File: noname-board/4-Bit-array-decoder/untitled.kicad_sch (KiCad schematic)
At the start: 16 parts, among them U1 CD4514BM

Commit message: hmmm
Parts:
- removed D1, D10, D11, D12, D13, D14, D15, D2, D3, D4, D5, D6, D7, D8, D9: LED, symbol Device:LED
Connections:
- net leds and resistors cus long/out_pin 13: now reaches U1.16 (S14)
- net leds and resistors cus long/out_pin 11: now reaches U1.19 (S11)
- net leds and resistors cus long/out_pin 8: now reaches U1.9 (S2)
- net leds and resistors cus long/out_pin 7: now reaches U1.8 (S3)
- net leds and resistors cus long/out_pin 10: now reaches U1.20 (S10)
- net leds and resistors cus long/out_pin 4: now reaches U1.18 (S8)
- net leds and resistors cus long/out_pin 9: now reaches U1.10 (S1)
- net leds and resistors cus long/out_pin 14: now reaches U1.13 (S13)
- net leds and resistors cus long/out_pin 12: now reaches U1.14 (S12)
- net leds and resistors cus long/out_pin 15: now reaches U1.15 (S15)
- net leds and resistors cus long/out_pin 5: now reaches U1.17 (S9)
- net leds and resistors cus long/out_pin 6: now reaches U1.4 (S7)
- net leds and resistors cus long/out_pin 2: now reaches U1.5 (S6)
- net leds and resistors cus long/out_pin 3: now reaches U1.6 (S5)
- net leds and resistors cus long/out_pin 1: now reaches U1.7 (S4)
- net power renamed 5V
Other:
- added sheet leds and resistors cus long (leds and resistors cus long.kicad_sch)

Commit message: commented on evan's thing
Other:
- note added: "so real"
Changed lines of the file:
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@@
     (stroke (width 0) (type default))
+  )
+  (text "so real\n" (at 165.1 116.84 0)
+    (effects (font (size 1.27 1.27)) (justify left bottom))
   )
   (global_label "GND" (shape input) (at 128.27 116.84 0) (fields_autoplaced)

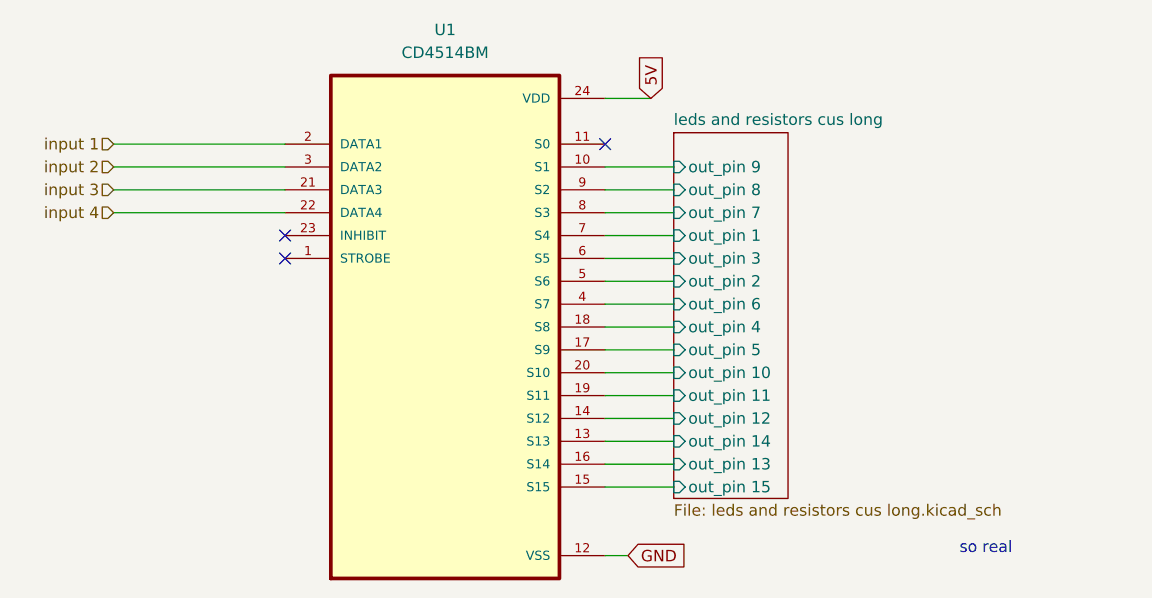
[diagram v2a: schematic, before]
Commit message: Changed Global to Hierarchals
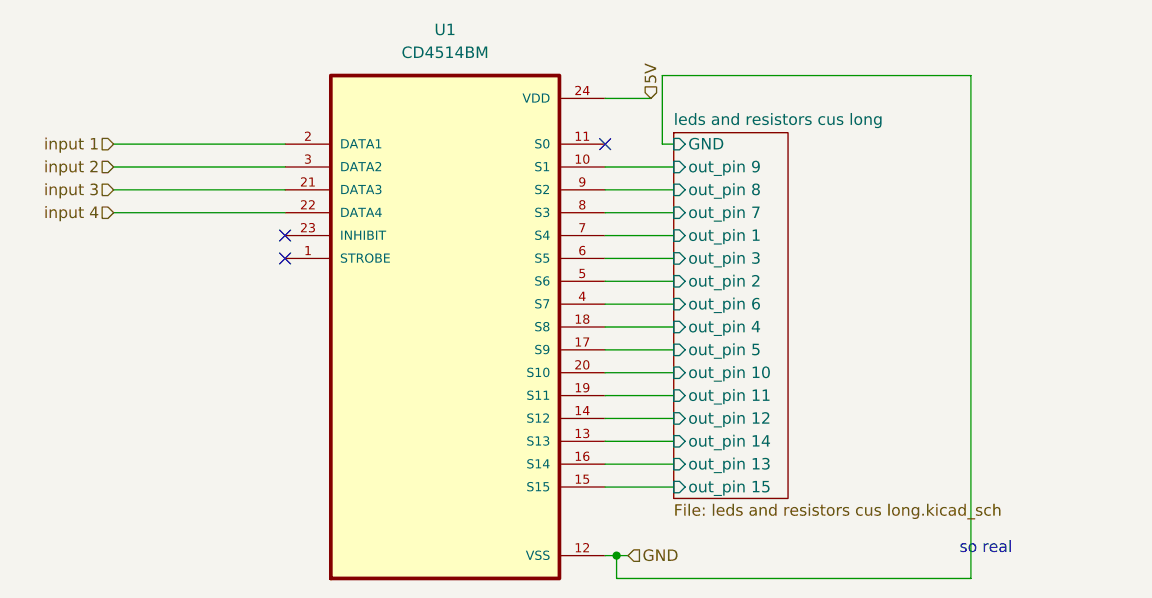
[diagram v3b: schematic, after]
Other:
- sheet leds and resistors cus long ports: added GND; removed none
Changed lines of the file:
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@@
 (kicad_sch (version 20230121) (generator eeschema)
   (paper "A4")
+  (junction (at 127 116.84) (diameter 0) (color 0 0 0 0)
+  )
   (no_connect (at 90.17 83.82))
   (no_connect (at 90.17 81.28))
@@
     (stroke (width 0) (type default))
   )
+  (wire (pts (xy 132.08 63.5) (xy 166.37 63.5))
+    (stroke (width 0) (type default))
+  )
+  (wire (pts (xy 127 116.84) (xy 128.27 116.84))
+    (stroke (width 0) (type default))
+  )
   (wire (pts (xy 125.73 81.28) (xy 133.35 81.28))
     (stroke (width 0) (type default))
@@
     (stroke (width 0) (type default))
   )
+  (wire (pts (xy 132.08 71.12) (xy 132.08 63.5))
+    (stroke (width 0) (type default))
+  )
   (wire (pts (xy 125.73 99.06) (xy 133.35 99.06))
     (stroke (width 0) (type default))
@@
     (stroke (width 0) (type default))
   )
+  (wire (pts (xy 166.37 119.38) (xy 127 119.38))
+    (stroke (width 0) (type default))
+  )
   (wire (pts (xy 125.73 101.6) (xy 133.35 101.6))
     (stroke (width 0) (type default))
@@
     (stroke (width 0) (type default))
   )
+  (wire (pts (xy 127 119.38) (xy 127 116.84))
+    (stroke (width 0) (type default))
+  )
+  (wire (pts (xy 133.35 71.12) (xy 132.08 71.12))
+    (stroke (width 0) (type default))
+  )
   (wire (pts (xy 125.73 109.22) (xy 133.35 109.22))
     (stroke (width 0) (type default))
   )
+  (wire (pts (xy 166.37 63.5) (xy 166.37 119.38))
+    (stroke (width 0) (type default))
+  )
   (wire (pts (xy 125.73 78.74) (xy 133.35 78.74))
     (stroke (width 0) (type default))
   )
-  (wire (pts (xy 125.73 116.84) (xy 128.27 116.84))
+  (wire (pts (xy 125.73 116.84) (xy 127 116.84))
     (stroke (width 0) (type default))
   )
@@
     (effects (font (size 1.27 1.27)) (justify left bottom))
   )
-  (global_label "GND" (shape input) (at 128.27 116.84 0) (fields_autoplaced)
+  (hierarchical_label "GND" (shape input) (at 128.27 116.84 0) (fields_autoplaced)
     (effects (font (size 1.27 1.27)) (justify left))
-    (property "Intersheetrefs" "${INTERSHEET_REFS}" (at 135.1257 116.84 0)
-      (effects (font (size 1.27 1.27)) (justify left) hide)
-    )
-  )
-  (global_label "5V" (shape input) (at 130.81 66.04 90) (fields_autoplaced)
+  )
+  (hierarchical_label "input 4" (shape input) (at 71.12 78.74 180) (fields_autoplaced)
+    (effects (font (size 1.27 1.27)) (justify right))
+  )
+  (hierarchical_label "5V" (shape input) (at 130.81 66.04 90) (fields_autoplaced)
     (effects (font (size 1.27 1.27)) (justify left))
-    (property "Intersheetrefs" "${INTERSHEET_REFS}" (at 130.81 60.7567 90)
-      (effects (font (size 1.27 1.27)) (justify left) hide)
-    )
-  )
-  (hierarchical_label "input 4" (shape input) (at 71.12 78.74 180) (fields_autoplaced)
-    (effects (font (size 1.27 1.27)) (justify right))
   )
   (hierarchical_label "input 2" (shape input) (at 71.12 73.66 180) (fields_autoplaced)
@@
       (effects (font (size 1.27 1.27)) (justify left))
     )
+    (pin "GND" input (at 133.35 71.12 180)
+      (effects (font (size 1.27 1.27)) (justify left))
+    )
